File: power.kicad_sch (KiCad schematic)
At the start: 1 part, among them M2 Module-power_12and5V-0.2

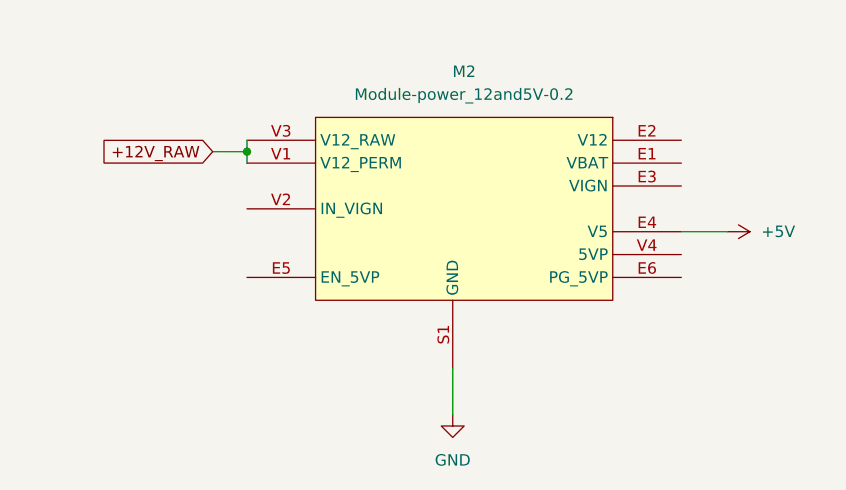
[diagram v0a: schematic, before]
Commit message: trying to fix aligment
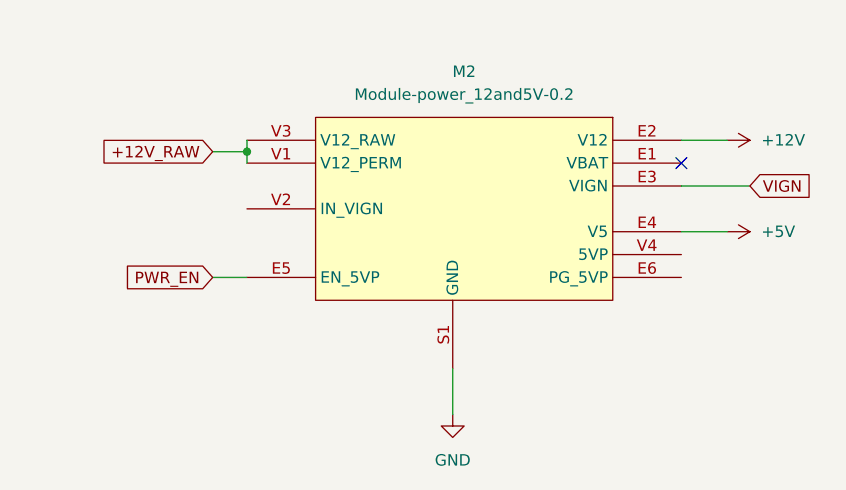
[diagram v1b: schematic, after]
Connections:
- net +12V: now reaches M2.E2 (V12)
- net VIGN: now reaches M2.E3 (VIGN)
- net PWR_EN: now reaches M2.E5 (EN_5VP)
- no-connect marks 0 -> 1
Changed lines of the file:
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@@
 		(color 0 0 0 0)
 	)
+	(no_connect
+		(at 156.21 73.66)
+	)
 	(wire
 		(pts
@@
 	(wire
 		(pts
+			(xy 156.21 71.12) (xy 161.29 71.12)
+		)
+		(stroke
+			(width 0)
+			(type default)
+		)
+	)
+	(wire
+		(pts
+			(xy 156.21 76.2) (xy 163.83 76.2)
+		)
+		(stroke
+			(width 0)
+			(type default)
+		)
+	)
+	(wire
+		(pts
 			(xy 104.14 72.39) (xy 107.95 72.39)
 		)
@@
 		(pts
 			(xy 156.21 81.28) (xy 161.29 81.28)
+		)
+		(stroke
+			(width 0)
+			(type default)
+		)
+	)
+	(wire
+		(pts
+			(xy 104.14 86.36) (xy 107.95 86.36)
 		)
 		(stroke
@@
 		(property "Intersheetrefs" "${INTERSHEET_REFS}"
 			(at 91.2972 72.39 0)
+			(effects
+				(font
+					(size 1.27 1.27)
+				)
+				(justify right)
+				(hide yes)
+			)
+		)
+	)
+	(global_label "VIGN"
+		(shape input)
+		(at 163.83 76.2 0)
+		(fields_autoplaced yes)
+		(effects
+			(font
+				(size 1.27 1.27)
+			)
+			(justify left)
+		)
+		(property "Intersheetrefs" "${INTERSHEET_REFS}"
+			(at 171.1091 76.2 0)
+			(effects
+				(font
+					(size 1.27 1.27)
+				)
+				(justify left)
+				(hide yes)
+			)
+		)
+	)
+	(global_label "PWR_EN"
+		(shape input)
+		(at 104.14 86.36 180)
+		(fields_autoplaced yes)
+		(effects
+			(font
+				(size 1.27 1.27)
+			)
+			(justify right)
+		)
+		(property "Intersheetrefs" "${INTERSHEET_REFS}"
+			(at 93.7163 86.36 0)
 			(effects
 				(font
@@
 					(unit 1)
 				)
+			)
+		)
+	)
+	(symbol
+		(lib_id "power:+12V")
+		(at 161.29 71.12 270)
+		(unit 1)
+		(exclude_from_sim no)
+		(in_bom yes)
+		(on_board yes)
+		(dnp no)
+		(fields_autoplaced yes)
+		(property "Reference" "#PWR022"
+			(at 157.48 71.12 0)
+			(effects
+				(font
+					(size 1.27 1.27)
+				)
+				(hide yes)
+			)
+		)
+		(property "Value" "+12V"
+			(at 165.1 71.1199 90)
+			(effects
+				(font
+					(size 1.27 1.27)
+				)
+				(justify left)
+			)
+		)
+		(property "Footprint" ""
+			(at 161.29 71.12 0)
+			(effects
+				(font
+					(size 1.27 1.27)
+				)
+				(hide yes)
+			)
+		)
+		(property "Datasheet" ""
+			(at 161.29 71.12 0)
+			(effects
+				(font
+					(size 1.27 1.27)
+				)
+				(hide yes)
+			)
+		)
+		(property "Description" "Power symbol creates a global label with name \"+12V\""
+			(at 161.29 71.12 0)
+			(effects
+				(font
+					(size 1.27 1.27)
+				)
+				(hide yes)
+			)
+		)
+		(pin "1"
+		)
+		(instances
+			(project ""
+				(path "/83409e39-90d0-4c85-be2e-bd292bea7c12/c821ec8f-5107-4775-a1b2-7b03d20e14b3"
+					(reference "#PWR022")
+					(unit 1)
+				)

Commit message: Implementing some inputs and outputs
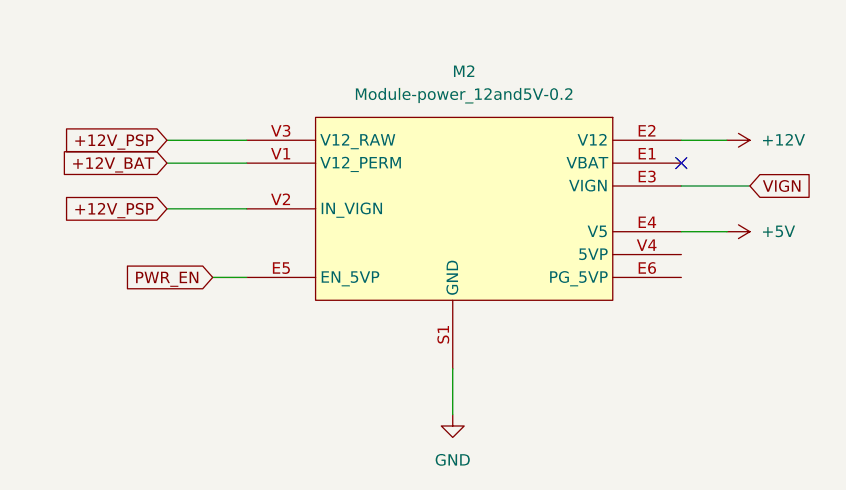
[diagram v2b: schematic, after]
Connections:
- net +12V_PSP: now reaches M2.V2 (IN_VIGN)
- net +12V_PSP: now also M2.V3 (V12_RAW)
- net +12V_RAW renamed +12V_BAT
- net +12V_BAT: no longer M2.V3 (V12_RAW)
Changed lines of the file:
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@@
 	(generator_version "8.0")
 	(paper "A4")
-	(junction
-		(at 107.95 72.39)
-		(diameter 0)
-		(color 0 0 0 0)
-	)
 	(no_connect
 		(at 156.21 73.66)
@@
 	(wire
 		(pts
-			(xy 107.95 71.12) (xy 107.95 72.39)
+			(xy 107.95 78.74) (xy 99.06 78.74)
 		)
 		(stroke
@@
 		(pts
 			(xy 130.81 96.52) (xy 130.81 101.6)
-		)
-		(stroke
-			(width 0)
-			(type default)
-		)
-	)
-	(wire
-		(pts
-			(xy 107.95 72.39) (xy 107.95 73.66)
 		)
 		(stroke
@@
 	(wire
 		(pts
-			(xy 104.14 72.39) (xy 107.95 72.39)
+			(xy 107.95 73.66) (xy 99.06 73.66)
+		)
+		(stroke
+			(width 0)
+			(type default)
+		)
+	)
+	(wire
+		(pts
+			(xy 107.95 71.12) (xy 99.06 71.12)
 		)
 		(stroke
@@
 		)
 	)
-	(global_label "+12V_RAW"
+	(global_label "+12V_PSP"
 		(shape input)
-		(at 104.14 72.39 180)
+		(at 99.06 71.12 180)
 		(fields_autoplaced yes)
 		(effects
@@
 		)
 		(property "Intersheetrefs" "${INTERSHEET_REFS}"
-			(at 91.2972 72.39 0)
+			(at 86.2777 71.12 0)
+			(effects
+				(font
+					(size 1.27 1.27)
+				)
+				(justify right)
+				(hide yes)
+			)
+		)
+	)
+	(global_label "+12V_BAT"
+		(shape input)
+		(at 99.06 73.66 180)
+		(fields_autoplaced yes)
+		(effects
+			(font
+				(size 1.27 1.27)
+			)
+			(justify right)
+		)
+		(property "Intersheetrefs" "${INTERSHEET_REFS}"
+			(at 86.701 73.66 0)
 			(effects
 				(font
@@
 				(hide yes)
 			)
+		)
+	)
+	(global_label "+12V_PSP"
+		(shape input)
+		(at 99.06 78.74 180)
+		(fields_autoplaced yes)
+		(effects
+			(font
+				(size 1.27 1.27)
+			)
+			(justify right)
+		)
+		(property "Intersheetrefs" "${INTERSHEET_REFS}"
+			(at 86.2777 78.74 0)
+			(effects
+				(font
+					(size 1.27 1.27)
+				)
+				(justify right)
+				(hide yes)
+			)

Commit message: trying out a layout and routing
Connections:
- net +12V_BAT: now also M2.V3 (V12_RAW)
- net +12V_PSP: no longer M2.V3 (V12_RAW)
- net +5VP: now reaches M2.V4 (5VP)
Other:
- note added: "TODO: PSP = IGNITION BASED?"
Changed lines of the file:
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@@
 	(generator_version "8.0")
 	(paper "A4")
+	(junction
+		(at 100.33 71.12)
+		(diameter 0)
+		(color 0 0 0 0)
+	)
 	(no_connect
 		(at 156.21 73.66)
@@
 	(wire
 		(pts
+			(xy 156.21 83.82) (xy 161.29 83.82)
+		)
+		(stroke
+			(width 0)
+			(type default)
+		)
+	)
+	(wire
+		(pts
 			(xy 107.95 78.74) (xy 99.06 78.74)
 		)
@@
 	(wire
 		(pts
+			(xy 100.33 73.66) (xy 107.95 73.66)
+		)
+		(stroke
+			(width 0)
+			(type default)
+		)
+	)
+	(wire
+		(pts
 			(xy 156.21 71.12) (xy 161.29 71.12)
 		)
@@
 	(wire
 		(pts
-			(xy 107.95 73.66) (xy 99.06 73.66)
-		)
-		(stroke
-			(width 0)
-			(type default)
-		)
-	)
-	(wire
-		(pts
-			(xy 107.95 71.12) (xy 99.06 71.12)
+			(xy 100.33 71.12) (xy 107.95 71.12)
+		)
+		(stroke
+			(width 0)
+			(type default)
+		)
+	)
+	(wire
+		(pts
+			(xy 100.33 71.12) (xy 100.33 73.66)
+		)
+		(stroke
+			(width 0)
+			(type default)
+		)
+	)
+	(wire
+		(pts
+			(xy 100.33 71.12) (xy 99.06 71.12)
 		)
 		(stroke
@@
 		)
 	)
-	(global_label "+12V_PSP"
+	(text "TODO: PSP = IGNITION BASED?"
+		(exclude_from_sim no)
+		(at 83.82 75.438 90)
+		(effects
+			(font
+				(size 1.27 1.27)
+			)
+		)
+	)
+	(global_label "+12V_BAT"
 		(shape input)
 		(at 99.06 71.12 180)
@@
 		)
 		(property "Intersheetrefs" "${INTERSHEET_REFS}"
-			(at 86.2777 71.12 0)
-			(effects
-				(font
-					(size 1.27 1.27)
-				)
-				(justify right)
-				(hide yes)
-			)
-		)
-	)
-	(global_label "+12V_BAT"
-		(shape input)
-		(at 99.06 73.66 180)
-		(fields_autoplaced yes)
-		(effects
-			(font
-				(size 1.27 1.27)
-			)
-			(justify right)
-		)
-		(property "Intersheetrefs" "${INTERSHEET_REFS}"
-			(at 86.701 73.66 0)
+			(at 86.701 71.12 0)
 			(effects
 				(font
@@
 					(unit 1)
 				)
+			)
+		)
+	)
+	(symbol
+		(lib_id "power:+5VP")
+		(at 161.29 83.82 270)
+		(unit 1)
+		(exclude_from_sim no)
+		(in_bom yes)
+		(on_board yes)
+		(dnp no)
+		(fields_autoplaced yes)
+		(property "Reference" "#PWR053"
+			(at 157.48 83.82 0)
+			(effects
+				(font
+					(size 1.27 1.27)
+				)
+				(hide yes)
+			)
+		)
+		(property "Value" "+5VP"
+			(at 165.1 83.8199 90)
+			(effects
+				(font
+					(size 1.27 1.27)
+				)
+				(justify left)
+			)
+		)
+		(property "Footprint" ""
+			(at 161.29 83.82 0)
+			(effects
+				(font
+					(size 1.27 1.27)
+				)
+				(hide yes)
+			)
+		)
+		(property "Datasheet" ""
+			(at 161.29 83.82 0)
+			(effects
+				(font
+					(size 1.27 1.27)
+				)
+				(hide yes)
+			)
+		)
+		(property "Description" "Power symbol creates a global label with name \"+5VP\""
+			(at 161.29 83.82 0)
+			(effects
+				(font
+					(size 1.27 1.27)
+				)
+				(hide yes)
+			)
+		)
+		(pin "1"
+		)
+		(instances
+			(project ""
+				(path "/83409e39-90d0-4c85-be2e-bd292bea7c12/c821ec8f-5107-4775-a1b2-7b03d20e14b3"
+					(reference "#PWR053")
+					(unit 1)
+				)

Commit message: redone layout, possibly feature complete
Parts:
- removed M2: Module-power_12and5V-0.2, 0.2:power_12and5V, symbol power_12and5V:Module-power_12and5V-0.2
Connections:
- no-connect marks 1 -> 0
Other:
- note removed: "TODO: PSP = IGNITION BASED?"
